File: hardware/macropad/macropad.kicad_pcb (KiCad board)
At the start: 2 copper layers, 6.5 x 0.7 mm, 83 parts, among them J1 SWD, J10 Conn_01x02, J2 USB_C_Receptacle_USB2.0_16P, J3 Conn_01x02, J4 display(4x1), J5 Conn_01x04_Pin, J6 Enc2, J7 Enc1, J8 Conn_01x02, J9 USB_A, Q1 Q_PMOS, Q2 FS8205A, SW1 SW_Push, SW12 SW_SPDT, SW13 SW_SPDT, SW2 SW_Push, SW3 SW_Push, SW4 SW_Push, SW5 SW_Push, SW6 SW_Push, SW7 SW_Push, SW8 SW_Push, SW9 SW_Push, U1 LP2992IM5-3.3/NOPB, U2 STM32F103C8Tx, U3 NRF24L01_Breakout, U4 STM32F103C8Tx, U5 NRF24L01_Breakout, U6 TP4056-42-ESOP8, U7 DW01A, U8 RT8010AGQW, U9 LP2992IM5-3.3/NOPB, Y1 8Mhz C_L=12pF, Y2 8Mhz

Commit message: updated. comments in whatsapp
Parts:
- C11, C12, C14, C16, C19, C20, C22, C23, C7, R3, R5: moved to B.Cu
- moved R7 116.0 mm to (54.9, 61.0)
- moved J8 115.5 mm to (71.3, 56.1)
- moved U6 115.4 mm to (67.8, 62.4)
- moved D1 115.3 mm to (74.4, 60.5)
- moved D2 115.3 mm to (67.8, 67.9)
- moved D3 115.3 mm to (74.4, 63.6)
- moved Q2 115.3 mm to (64.4, 56.7)
- moved R10 115.3 mm to (65.3, 48.1)
- moved R13 115.3 mm to (65.3, 50.7)
- moved R14 115.3 mm to (65.3, 53.2)
- moved R8 115.3 mm to (65.3, 43.1)
- moved R9 115.3 mm to (65.3, 45.6)
- moved U7 115.3 mm to (54.7, 69.6)
- moved C24 115.3 mm to (61.3, 43.1)
- moved C25 115.3 mm to (61.3, 45.6)
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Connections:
- net /dongle/USB_D+_DGL renamed /dongle/USB_D_DGL+
- net /dongle/USB_D-_DGL renamed /dongle/USB_D_DGL-
- Q1 pad 1: (no net) -> VBUS
- Q1 pad 2: (no net) -> out+
- Q1 pad 3: (no net) -> Net-(Q1-D)
- SW12 pad 2: Net-(SW12-B) -> Net-(Q1-D)
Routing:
- net GND_DGL: track 0.00 -> 61.8 mm, vias 0 -> 3
- net /dongle/SWDIO_DGL: track 0.00 -> 45.3 mm
- net /dongle/SWCLK_DGL: track 0.00 -> 37.0 mm
- net +3.3V_DGL: track 0.00 -> 36.7 mm, vias 0 -> 6
- net /dongle/NRST_DGL: track 0.00 -> 16.2 mm, vias 0 -> 1
- net VBUS_DGL: track 0.00 -> 16.0 mm
- net /dongle/USB_D_DGL-: track 0.00 -> 9.90 mm
- net /dongle/USB_D_DGL+: track 0.00 -> 9.90 mm
- net /dongle/HSE_IN_DGL: track 0.00 -> 4.79 mm
- net /dongle/HSE_OUT_DGL: track 0.00 -> 2.96 mm
- net Net-(U1-BYP): track 0.00 -> 2.41 mm, vias 0 -> 1
- net /dongle/BOOT0_DGL: track 0.00 -> 1.81 mm, vias 0 -> 1
- net /dongle/BOOT1_DGL: track 0.00 -> 1.63 mm, vias 0 -> 1
- added copper zone on F.Cu, net +3.3V_DGL
- added copper zone on B.Cu, net GND_DGL
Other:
- board size 6.5 x 0.7 mm -> 157.2 x 88.1 mm

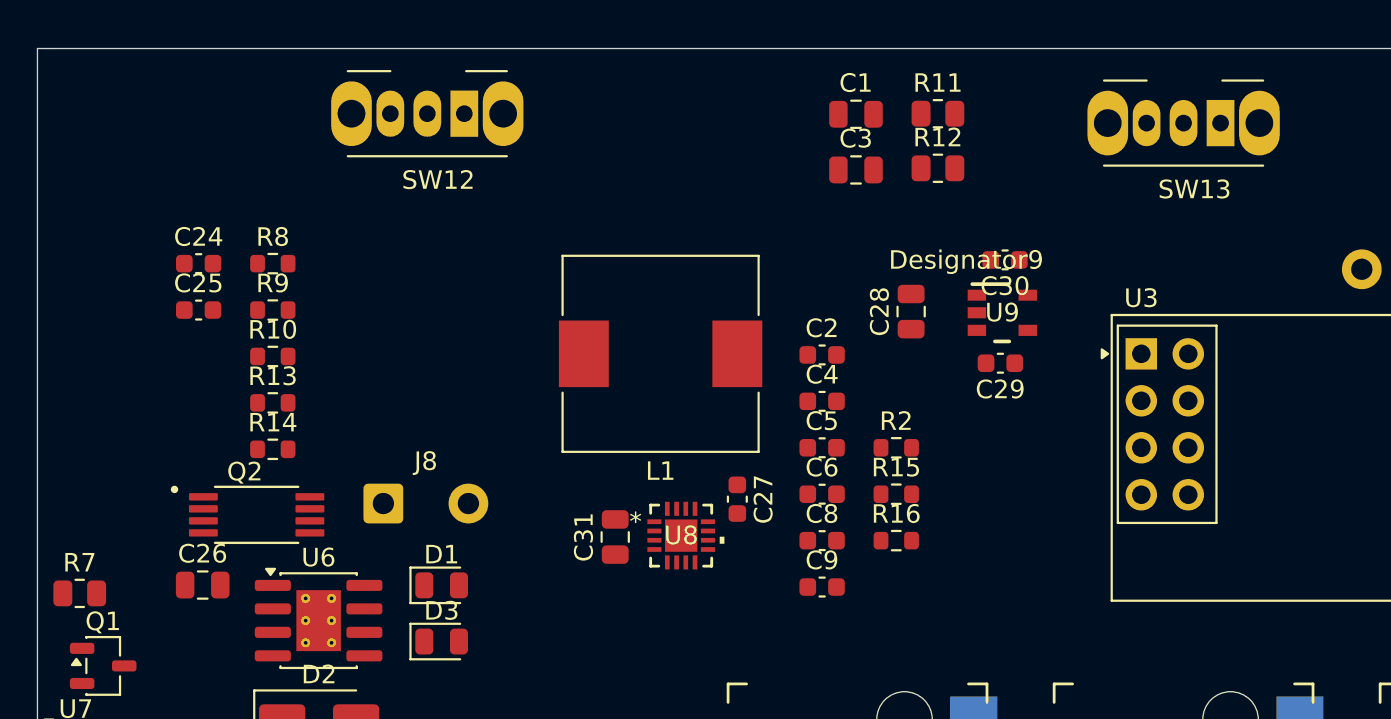
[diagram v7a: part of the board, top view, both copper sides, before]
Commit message: updated pcb with switch
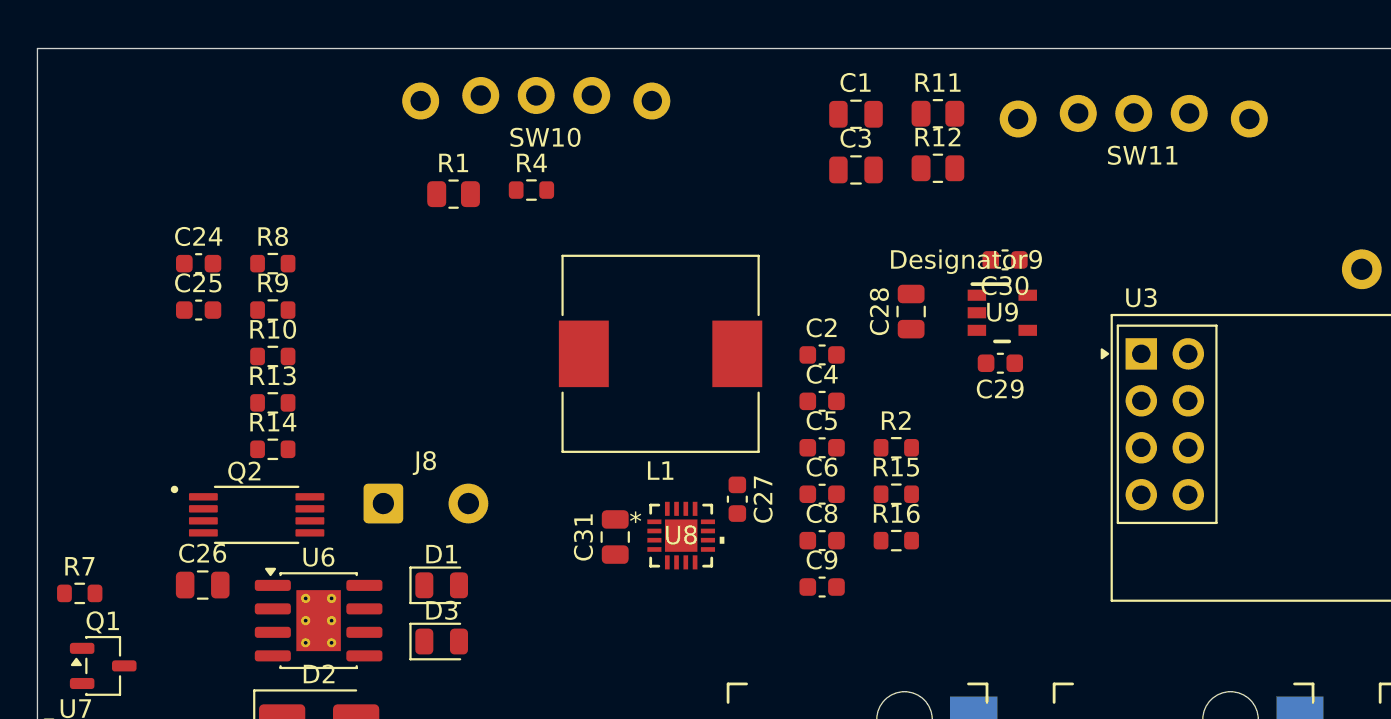
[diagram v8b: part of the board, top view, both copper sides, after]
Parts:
- removed SW12, SW13: SW_SPDT, Button_Switch_THT:SW_Slide_SPDT_Angled_CK_OS102011MA1Q
- added R1: 10k, Resistor_SMD:R_0805_2012Metric, F.Cu at (75.1, 39.4)
- added R4: 1k, Resistor_SMD:R_0603_1608Metric, F.Cu at (79.3, 39.1)
- added SW10: SW_SPDT, SS12F23L5:SS12F23L5 spdt, F.Cu at (79.5, 34.3)
- added SW11: SW_SPDT, SS12F23L5:SS12F23L5 spdt, F.Cu at (111.9, 35.3)
- R10: value 1.2k -> 100
- R7: value 10k -> 1k; footprint Resistor_SMD:R_0805_2012Metric -> Resistor_SMD:R_0603_1608Metric
- R8: value 1k -> 1.2k
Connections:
- R10 pad 1: Net-(U6-PROG) -> Net-(U7-VCC)
- R10 pad 2: GND -> /Power/B+
- R7 pad 1: VBUS -> Net-(U6-~{STDBY})
- R7 pad 2: GND -> Net-(D3-K)
- R8 pad 1: Net-(U6-~{CHRG}) -> Net-(U6-PROG)
- R8 pad 2: Net-(D1-K) -> GND
- R9 pad 1: Net-(U6-~{STDBY}) -> Net-(U7-CS)
- R9 pad 2: Net-(D3-K) -> /Power/out-
